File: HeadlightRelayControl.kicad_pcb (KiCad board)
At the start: 2 copper layers, 49.5 x 49.5 mm, 42 parts, among them P1 CONN_01X03, P2 CONN_2, P3 CONN_01X02, P4 CONN_01X02, Q1 2N3904, Q2 2N3904, Q3 2N3904, Q4 2N3904, Q5 2N3904, Q6 2N3904

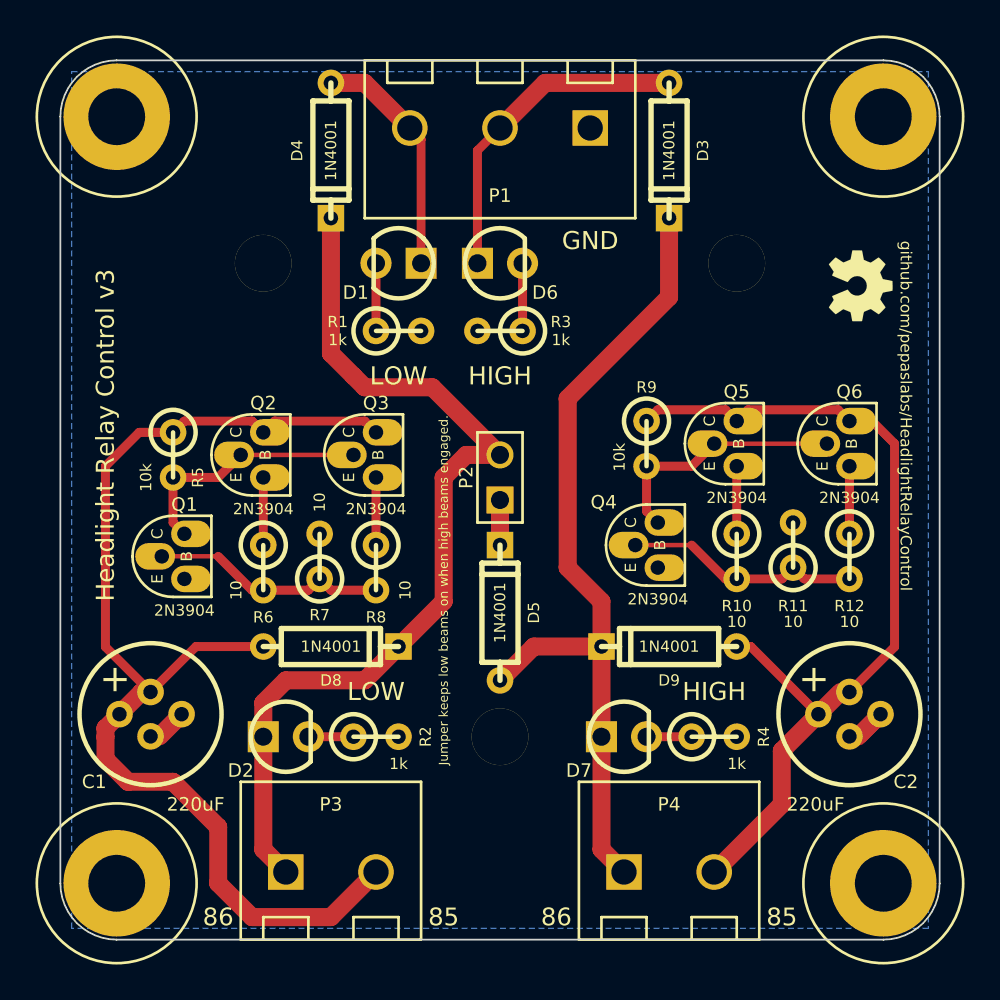
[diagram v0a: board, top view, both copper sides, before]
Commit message: changing 1N4001 diodes to schottky 1N5817. updating diode footprints. adding substitution notes to schematic.
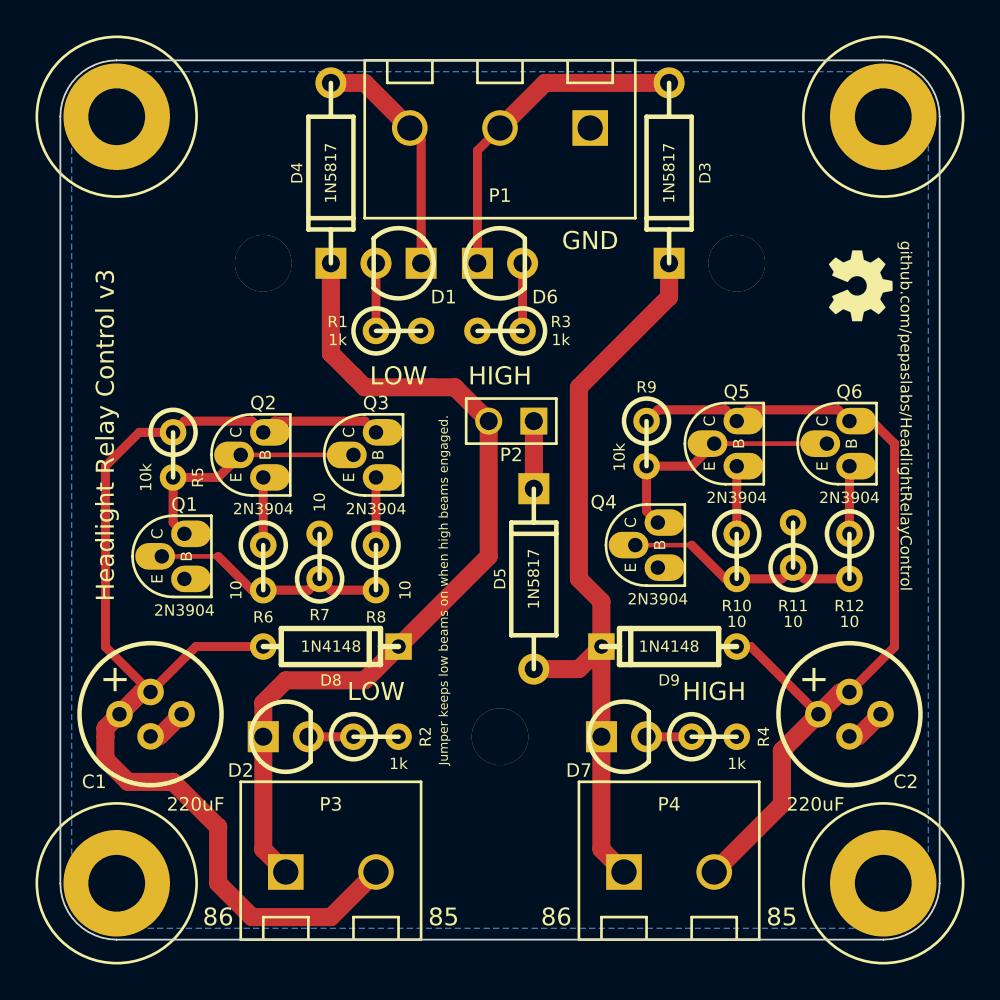
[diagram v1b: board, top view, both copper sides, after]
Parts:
- D3, D4, D5: value 1N4001 -> 1N5817; footprint DIODE_3_059A -> DIODE_1A_069A_PL
- D8, D9: value 1N4001 -> 1N4148
- moved D5 6.02 mm to (110.5, 95.2)
- moved D3 5.08 mm to (118.1, 72.4)
- moved D4 5.08 mm to (99.1, 72.4)
- moved P2 3.24 mm to (109.2, 86.4), turned to 180 degrees
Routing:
- net HighBeamControl: track 47.0 -> 41.8 mm
- net LowBeamControl: track 52.8 -> 49.3 mm
- net N-0000028: track 2.54 -> 3.81 mm
